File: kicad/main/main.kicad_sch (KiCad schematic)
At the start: 5 parts

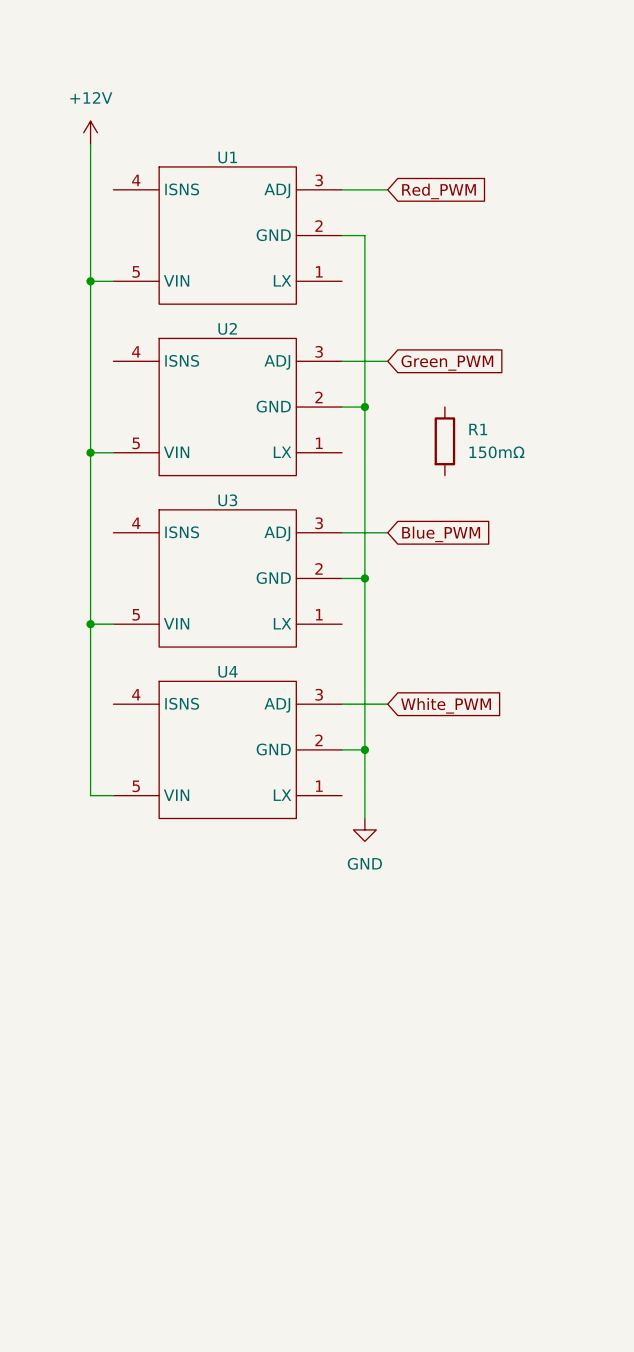
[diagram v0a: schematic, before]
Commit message: Started working on CC regulators
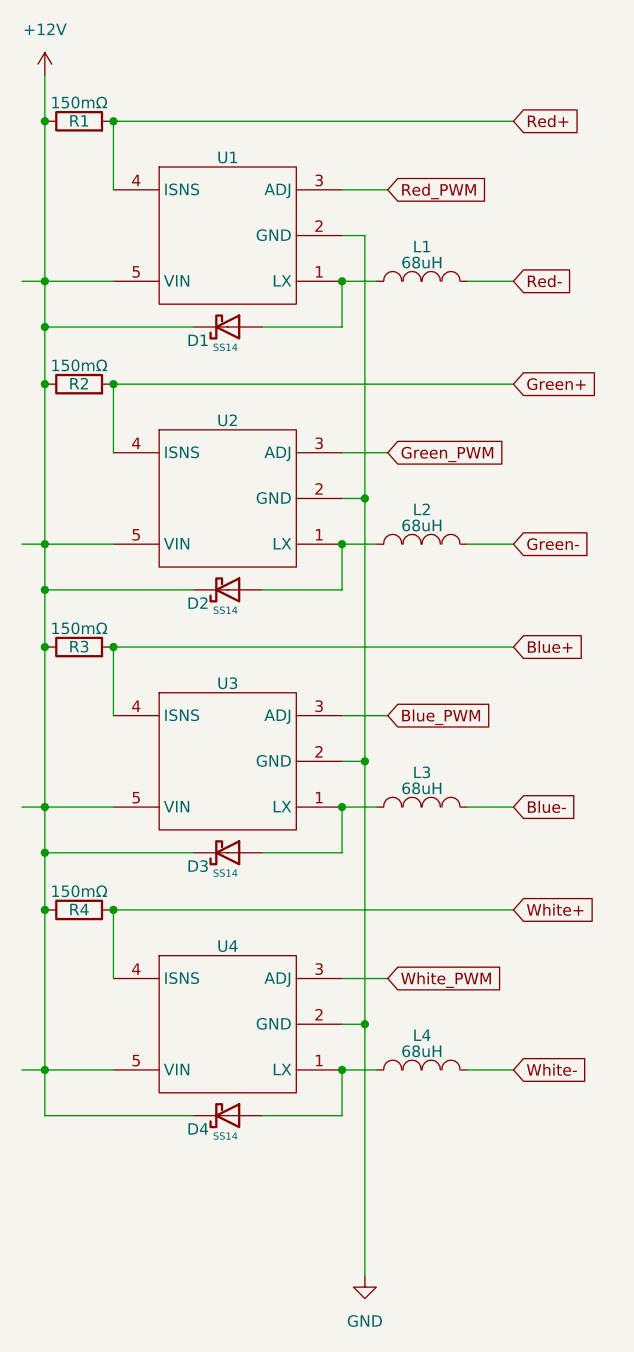
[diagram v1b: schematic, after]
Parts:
- added D1, D2, D3, D4: SS14, PCM_JLCPCB:D_SMA, symbol PCM_JLCPCB-Diodes:Schottky,SS14
- added L1, L2, L3, L4: 68uH, EasyEDA_Lib:IND-SMD_L6.0-W6.0_FNR60XXS, symbol EasyEDA_Lib:FNR6045S680MT
- added R2, R3, R4: 150mΩ, Resistor_SMD:R_1206_3216Metric_Pad1.30x1.75mm_HandSolder, symbol Device:R
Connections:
- net +12V: now also R1.1, D1.1, D2.1, D3.1, D4.1, R2.1, R3.1, R4.1
- net Red+: now reaches R1.2
- net Red+: now also U1.4 (ISNS)
- net at U3.1 (LX): now also D3.2, L3.1
- net Blue+: now reaches U3.4 (ISNS)
- net Blue+: now also R3.2
- net at U4.1 (LX): now also D4.2, L4.1
- net White+: now reaches U4.4 (ISNS)
- net White+: now also R4.2
- net at U1.1 (LX): now also D1.2, L1.1
- net at U2.1 (LX): now also D2.2, L2.1
- net Green+: now reaches U2.4 (ISNS)
- net Green+: now also R2.2
- new net Blue-: L3.2
- new net Green-: L2.2
- new net Red-: L1.2
- new net White-: L4.2
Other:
- moved on the sheet: R1
